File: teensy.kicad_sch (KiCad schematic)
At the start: 6 parts

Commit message: V0.1
really jjust updating a bunch of stuff
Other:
- note added: "BUS STUFF STILL NEEDED"
- title: (none) -> VMC-1
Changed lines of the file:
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@@
   (paper "USLetter")
   (title_block
-    (date "2023-12-01")
+    (title "VMC-1")
+    (date "2023-12-03")
     (rev "1.00")
+  )
+  (bus_entry (at 95.25 83.82) (size -2.54 -2.54)
+    (stroke (width 0) (type default))
+  )
+  (bus_entry (at 95.25 86.36) (size -2.54 -2.54)
+    (stroke (width 0) (type default))
+  )
+  (bus_entry (at 95.25 88.9) (size -2.54 -2.54)
+    (stroke (width 0) (type default))
   )
   (wire (pts (xy 56.515 93.98) (xy 56.515 107.95))
@@
     (stroke (width 0) (type default))
   )
+  (bus (pts (xy 88.9 76.835) (xy 92.71 76.835))
+    (stroke (width 0) (type default))
+  )
   (wire (pts (xy 114.3 99.06) (xy 77.47 99.06))
     (stroke (width 0) (type default))
   )
   (wire (pts (xy 170.18 73.66) (xy 175.26 73.66))
+    (stroke (width 0) (type default))
+  )
+  (bus (pts (xy 92.71 83.82) (xy 92.71 86.36))
     (stroke (width 0) (type default))
   )
@@
     (stroke (width 0) (type default))
   )
+  (bus (pts (xy 92.71 76.835) (xy 92.71 81.28))
+    (stroke (width 0) (type default))
+  )
   (wire (pts (xy 138.43 147.32) (xy 138.43 143.51))
+    (stroke (width 0) (type default))
+  )
+  (bus (pts (xy 92.71 81.28) (xy 92.71 83.82))
     (stroke (width 0) (type default))
   )
@@
     (effects (font (size 1.27 1.27)) (justify left bottom))
   )
+  (text "BUS STUFF STILL NEEDED\n" (at 71.755 70.485 0)
+    (effects (font (size 1.27 1.27)) (justify left bottom))
+  )

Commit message: First Round ERC Checks
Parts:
- gave numbers to parts that had none: 2
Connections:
- net at RV?.2: now also U1.19 (27_A13_SCK1); no longer U1.18 (26_A12_MOSI1)
- net BLANK: now reaches U1.4 (2_OUT2)
- net XLAT: now reaches U1.5 (3_LRCLK2)
- net GSCLK: now reaches U1.7 (5_IN2)
- net SIN: now reaches U1.8 (6_OUT1D)
- net SCLK: now reaches U1.9 (7_RX2_OUT1A)
- net at RV?.2: now also U1.18 (26_A12_MOSI1)
- no-connect marks 0 -> 2
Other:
- note added: "More Info Here"
- note added: "SCLK is sensitive to signal overshoot. might need a risistor for long traces"
- note removed: "BUS STUFF STILL NEEDED"
- moved on the sheet: RV?

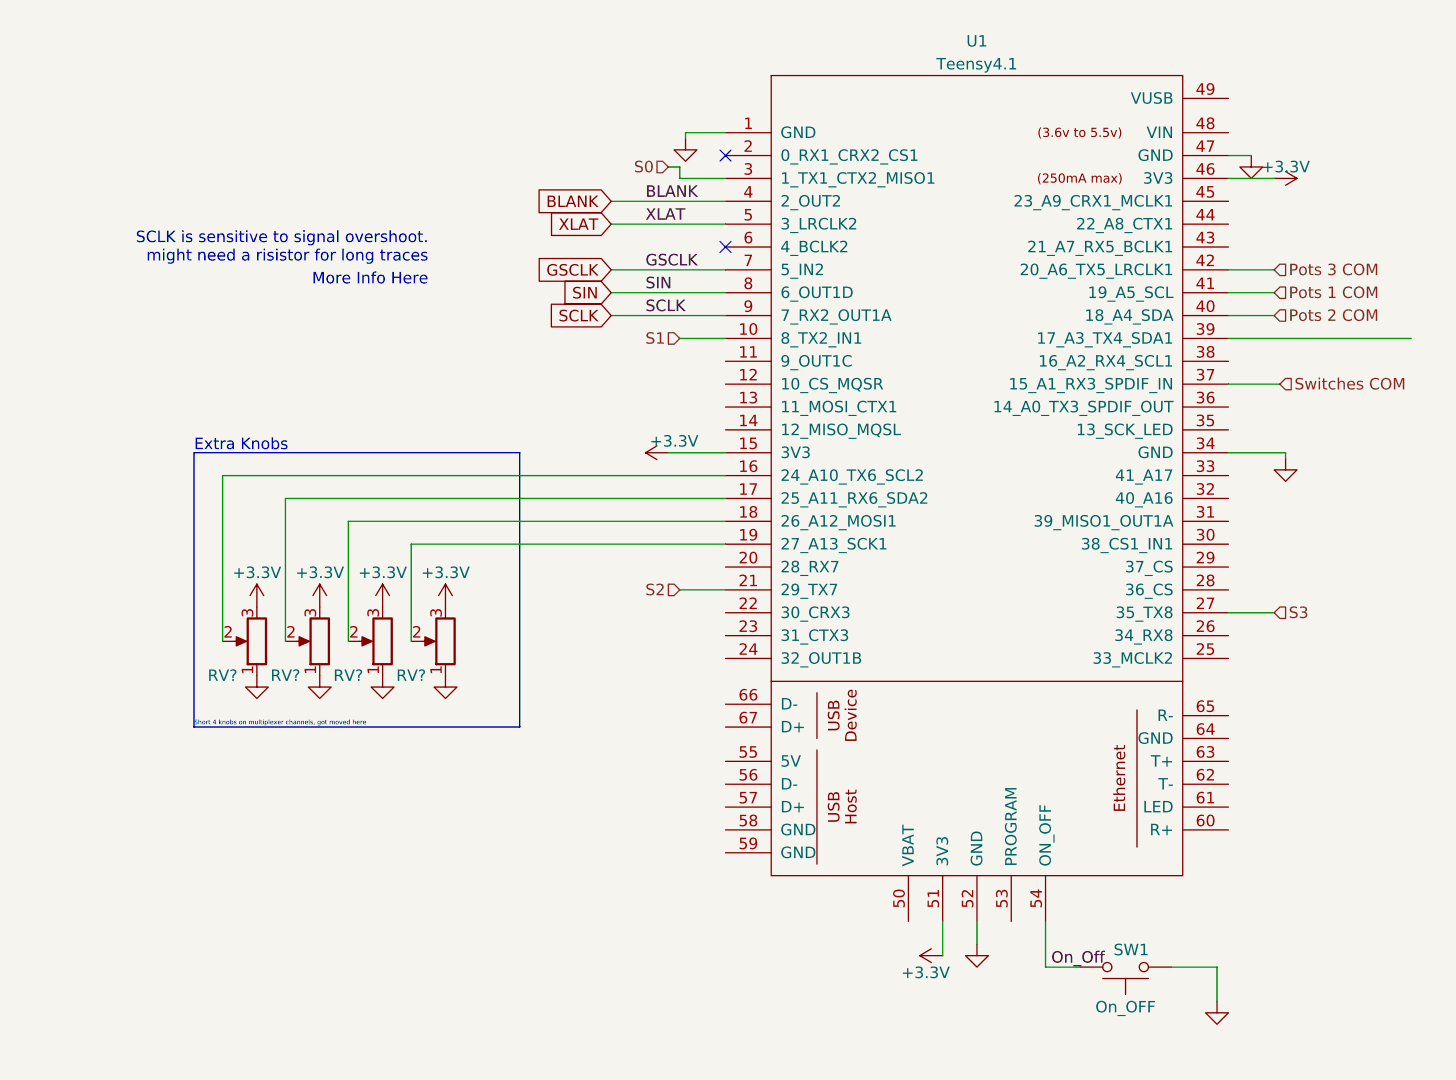
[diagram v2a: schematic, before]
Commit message: ERC Fixes
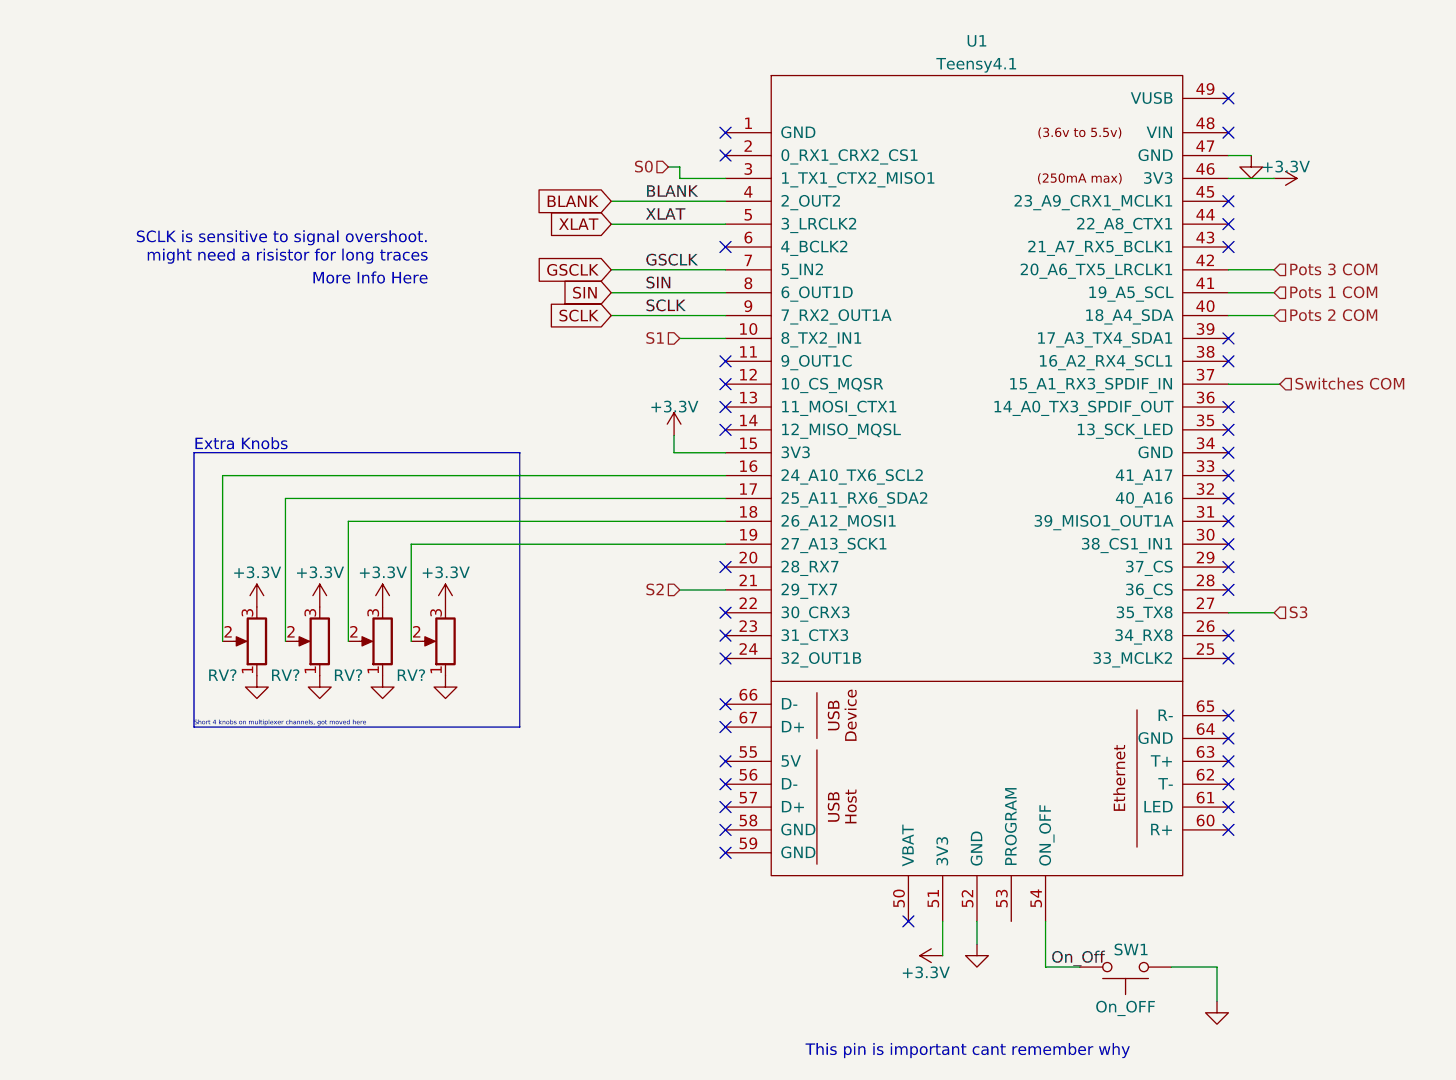
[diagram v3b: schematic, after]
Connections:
- net GND: no longer U1.1 (GND), U1.34 (GND)
- no-connect marks 2 -> 43
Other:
- note added: "This pin is important cant remember why"
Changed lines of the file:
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@@
     (rev "1.00")
   )
+  (no_connect (at 170.18 81.28))
+  (no_connect (at 114.3 81.28))
+  (no_connect (at 114.3 128.27))
+  (no_connect (at 114.3 104.14))
+  (no_connect (at 170.18 114.3))
+  (no_connect (at 114.3 55.88))
+  (no_connect (at 170.18 123.19))
+  (no_connect (at 170.18 130.81))
+  (no_connect (at 170.18 93.98))
+  (no_connect (at 170.18 104.14))
+  (no_connect (at 170.18 106.68))
+  (no_connect (at 114.3 83.82))
+  (no_connect (at 170.18 133.35))
+  (no_connect (at 170.18 120.65))
+  (no_connect (at 170.18 128.27))
+  (no_connect (at 170.18 101.6))
+  (no_connect (at 170.18 86.36))
+  (no_connect (at 114.3 111.76))
+  (no_connect (at 170.18 68.58))
+  (no_connect (at 170.18 88.9))
+  (no_connect (at 114.3 125.73))
   (no_connect (at 114.3 68.58))
+  (no_connect (at 170.18 52.07))
+  (no_connect (at 114.3 86.36))
+  (no_connect (at 114.3 119.38))
+  (no_connect (at 114.3 114.3))
+  (no_connect (at 114.3 133.35))
+  (no_connect (at 170.18 66.04))
+  (no_connect (at 170.18 55.88))
+  (no_connect (at 114.3 121.92))
+  (no_connect (at 170.18 78.74))
+  (no_connect (at 134.62 143.51))
   (no_connect (at 114.3 58.42))
+  (no_connect (at 170.18 99.06))
+  (no_connect (at 170.18 111.76))
+  (no_connect (at 170.18 125.73))
+  (no_connect (at 114.3 109.22))
+  (no_connect (at 114.3 130.81))
+  (no_connect (at 170.18 96.52))
+  (no_connect (at 114.3 88.9))
+  (no_connect (at 170.18 63.5))
+  (no_connect (at 114.3 135.89))
+  (no_connect (at 170.18 91.44))
+  (wire (pts (xy 108.585 91.44) (xy 114.3 91.44))
+    (stroke (width 0) (type default))
+  )
   (wire (pts (xy 142.24 146.05) (xy 142.24 143.51))
     (stroke (width 0) (type default))
@@
     (stroke (width 0) (type default))
   )
-  (wire (pts (xy 114.3 55.88) (xy 109.855 55.88))
-    (stroke (width 0) (type default))
-  )
   (wire (pts (xy 58.42 93.98) (xy 58.42 112.395))
     (stroke (width 0) (type default))
   )
-  (wire (pts (xy 176.53 91.44) (xy 176.53 92.075))
-    (stroke (width 0) (type default))
-  )
   (wire (pts (xy 79.375 101.6) (xy 79.375 112.395))
     (stroke (width 0) (type default))
@@
     (stroke (width 0) (type default))
   )
-  (wire (pts (xy 107.95 91.44) (xy 114.3 91.44))
-    (stroke (width 0) (type default))
-  )
   (wire (pts (xy 109.22 78.74) (xy 114.3 78.74))
     (stroke (width 0) (type default))
@@
     (stroke (width 0) (type default))
   )
+  (wire (pts (xy 108.585 89.535) (xy 108.585 91.44))
+    (stroke (width 0) (type default))
+  )
   (wire (pts (xy 65.405 96.52) (xy 65.405 112.395))
     (stroke (width 0) (type default))
@@
     (stroke (width 0) (type default))
   )
-  (wire (pts (xy 170.18 91.44) (xy 176.53 91.44))
-    (stroke (width 0) (type default))
-  )
   (wire (pts (xy 107.95 59.69) (xy 109.22 59.69))
     (stroke (width 0) (type default))
@@
     (stroke (width 0) (type default))
   )
-  (wire (pts (xy 109.855 55.88) (xy 109.855 56.515))
-    (stroke (width 0) (type default))
-  )
   (wire (pts (xy 149.86 143.51) (xy 149.86 148.59))
     (stroke (width 0) (type default))
@@
   )
   (wire (pts (xy 170.18 60.96) (xy 175.26 60.96))
-    (stroke (width 0) (type default))
-  )
-  (wire (pts (xy 170.18 78.74) (xy 190.5 78.74))
     (stroke (width 0) (type default))
   )
@@
   (text "More Info Here" (at 81.28 73.025 0)
     (effects (font (size 1.27 1.27)) (justify right bottom) (href "https://forum.pjrc.com/index.php?threads/sparkfun-tlc5940-and-teensy-4-0.71009/&p=323766&viewfull=1#post323766"))
+  )
+  (text "This pin is important cant remember why\n" (at 123.19 158.75 0)
+    (effects (font (size 1.27 1.27)) (justify left bottom))
   )
   (label "SIN" (at 105.41 73.66 0) (fields_autoplaced)
@@
     )
   )
-  (symbol (lib_id "power:+3.3V") (at 107.95 91.44 90) (unit 1)
-    (in_bom yes) (on_board yes) (dnp no)
-    (property "Reference" "#PWR04" (at 111.76 91.44 0)
-      (effects (font (size 1.27 1.27)) hide)
-    )
-    (property "Value" "+3.3V" (at 108.585 90.17 90)
-      (effects (font (size 1.27 1.27)))
-    )
-    (property "Footprint" "" (at 107.95 91.44 0)
-      (effects (font (size 1.27 1.27)) hide)
-    )
-    (property "Datasheet" "" (at 107.95 91.44 0)
-      (effects (font (size 1.27 1.27)) hide)
-    )
-    (pin "1")
-    (instances
-      (project "VMC1"
-        (path "/030598bf-3d55-483a-af42-40ff6f2e377a/fdfac26c-d8b4-497d-932c-b6e328b66f3b"
-          (reference "#PWR04") (unit 1)
-        )
-      )
-      (project "V"
-        (path "/f9418f3a-fa41-4a3d-8541-c10ffd215f7d/a637aa4d-93de-4cff-b28d-61c3ce6fea3c"
-          (reference "#PWR075") (unit 1)
-        )
-      )
-    )
-  )
   (symbol (lib_id "Device:R_Potentiometer") (at 69.215 112.395 180) (unit 1)
     (in_bom yes) (on_board yes) (dnp no)
@@
         (path "/f9418f3a-fa41-4a3d-8541-c10ffd215f7d/7ffcc307-6cac-4824-b607-a8f1674c733d"
           (reference "#PWR09") (unit 1)
-        )
-      )
-    )
-  )
-  (symbol (lib_id "power:GND") (at 176.53 92.075 0) (unit 1)
-    (in_bom yes) (on_board yes) (dnp no) (fields_autoplaced)
-    (property "Reference" "#PWR05" (at 176.53 98.425 0)
-      (effects (font (size 1.27 1.27)) hide)
-    )
-    (property "Value" "GND" (at 176.53 96.52 0)
-      (effects (font (size 1.27 1.27)) hide)
-    )
-    (property "Footprint" "" (at 176.53 92.075 0)
-      (effects (font (size 1.27 1.27)) hide)
-    )
-    (property "Datasheet" "" (at 176.53 92.075 0)
-      (effects (font (size 1.27 1.27)) hide)
-    )
-    (pin "1")
-    (instances
-      (project "VMC1"
-        (path "/030598bf-3d55-483a-af42-40ff6f2e377a/fdfac26c-d8b4-497d-932c-b6e328b66f3b"
-          (reference "#PWR05") (unit 1)
         )
       )
@@
     )
   )
-  (symbol (lib_id "power:GND") (at 109.855 56.515 0) (unit 1)
+  (symbol (lib_id "power:+3.3V") (at 108.585 89.535 0) (unit 1)
     (in_bom yes) (on_board yes) (dnp no) (fields_autoplaced)
-    (property "Reference" "#PWR01" (at 109.855 62.865 0)
-      (effects (font (size 1.27 1.27)) hide)
-    )
-    (property "Value" "GND" (at 109.855 61.595 0)
-      (effects (font (size 1.27 1.27)) hide)
-    )
-    (property "Footprint" "" (at 109.855 56.515 0)
-      (effects (font (size 1.27 1.27)) hide)
-    )
-    (property "Datasheet" "" (at 109.855 56.515 0)
+    (property "Reference" "#PWR01" (at 108.585 93.345 0)
+      (effects (font (size 1.27 1.27)) hide)
+    )
+    (property "Value" "+3.3V" (at 108.585 86.36 0)
+      (effects (font (size 1.27 1.27)))
+    )
+    (property "Footprint" "" (at 108.585 89.535 0)
+      (effects (font (size 1.27 1.27)) hide)
+    )
+    (property "Datasheet" "" (at 108.585 89.535 0)
       (effects (font (size 1.27 1.27)) hide)
     )
@@
         )
       )
-      (project "V"
-        (path "/f9418f3a-fa41-4a3d-8541-c10ffd215f7d/a637aa4d-93de-4cff-b28d-61c3ce6fea3c"
-          (reference "#PWR078") (unit 1)
-        )
-      )

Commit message: Post Kicad Community Telling Me Shit is Wrong
way more stuff needs love, DECOUPERS DUMA88s
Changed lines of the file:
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@@
+    (stroke (width 0) (type default))
+  )
+  (wire (pts (xy 179.705 60.96) (xy 170.18 60.96))
     (stroke (width 0) (type default))
   )
@@
     (stroke (width 0) (type default))
   )
+  (wire (pts (xy 179.705 57.785) (xy 179.705 60.96))
+    (stroke (width 0) (type default))
+  )
   (wire (pts (xy 109.22 78.74) (xy 114.3 78.74))
     (stroke (width 0) (type default))
@@
   )
   (wire (pts (xy 65.405 96.52) (xy 114.3 96.52))
-    (stroke (width 0) (type default))
-  )
-  (wire (pts (xy 170.18 60.96) (xy 175.26 60.96))
     (stroke (width 0) (type default))
   )
@@
     )
   )
-  (symbol (lib_id "power:+3.3V") (at 175.26 60.96 270) (unit 1)
+  (symbol (lib_id "power:+3.3V") (at 179.705 57.785 0) (unit 1)
     (in_bom yes) (on_board yes) (dnp no)
-    (property "Reference" "#PWR03" (at 171.45 60.96 0)
-      (effects (font (size 1.27 1.27)) hide)
-    )
-    (property "Value" "+3.3V" (at 176.53 59.69 90)
-      (effects (font (size 1.27 1.27)))
-    )
-    (property "Footprint" "" (at 175.26 60.96 0)
-      (effects (font (size 1.27 1.27)) hide)
-    )
-    (property "Datasheet" "" (at 175.26 60.96 0)
-      (effects (font (size 1.27 1.27)) hide)
-    )
+    (property "Reference" "#PWR03" (at 179.705 61.595 0)
+      (effects (font (size 1.27 1.27)) hide)
+    )
+    (property "Value" "+3.3V" (at 178.435 56.515 90)
+      (effects (font (size 1.27 1.27)))
+    )
+    (property "Footprint" "" (at 179.705 57.785 0)
+      (effects (font (size 1.27 1.27)) hide)
+    )
+    (property "Datasheet" "" (at 179.705 57.785 0)
+      (effects (font (size 1.27 1.27)) hide)
+    )
